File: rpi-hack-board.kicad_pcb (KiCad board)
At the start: 2 copper layers, 65 x 30 mm, 38 parts, among them J1 LOAD, J2 I2C_0, J3 I2C_1, J4 Raspberry_Pi_2_3, J5 PWR, J6 APA102, J7 SERIAL, J8 BREAKOUTS, Q1 TIP120, U1 DS1307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

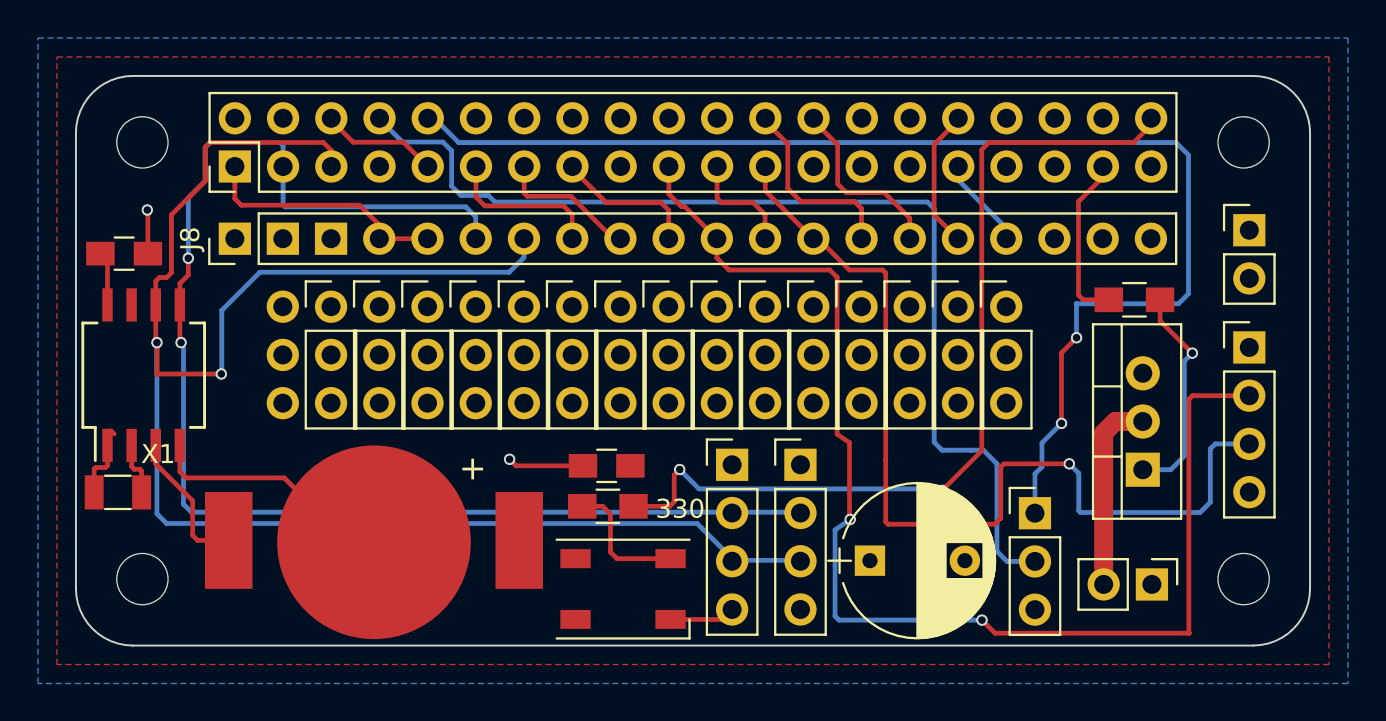
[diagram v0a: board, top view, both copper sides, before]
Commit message: Got a good start on the silkscreen layer, but there is loads to do.
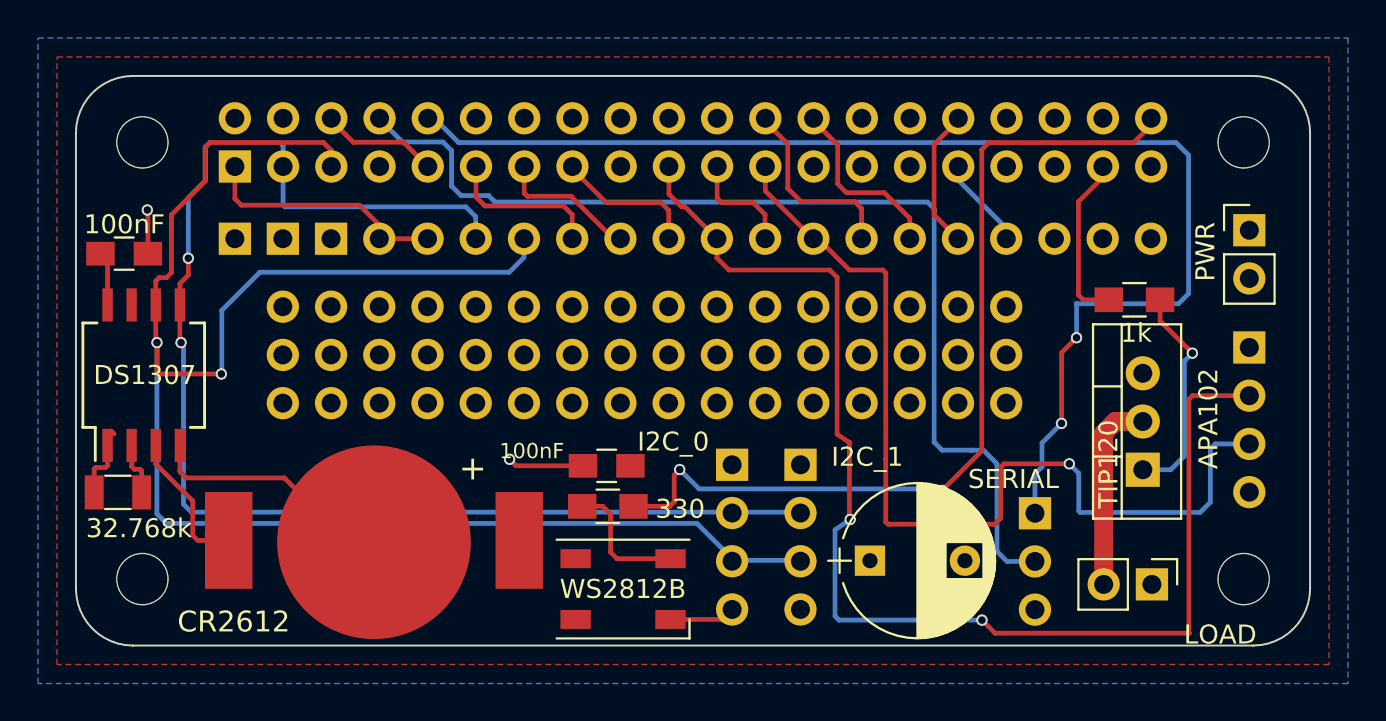
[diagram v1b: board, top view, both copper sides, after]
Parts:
- X1: value CRYSTAL -> 32.768k
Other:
- board text added: "5V"
- board text added: "CO"
- board text added: "CR2612"
- board text added: "GND"
- board text added: "RX"
- board text added: "SCL"
- board text added: "SDA"
- board text added: "SO"
- board text added: "TX"

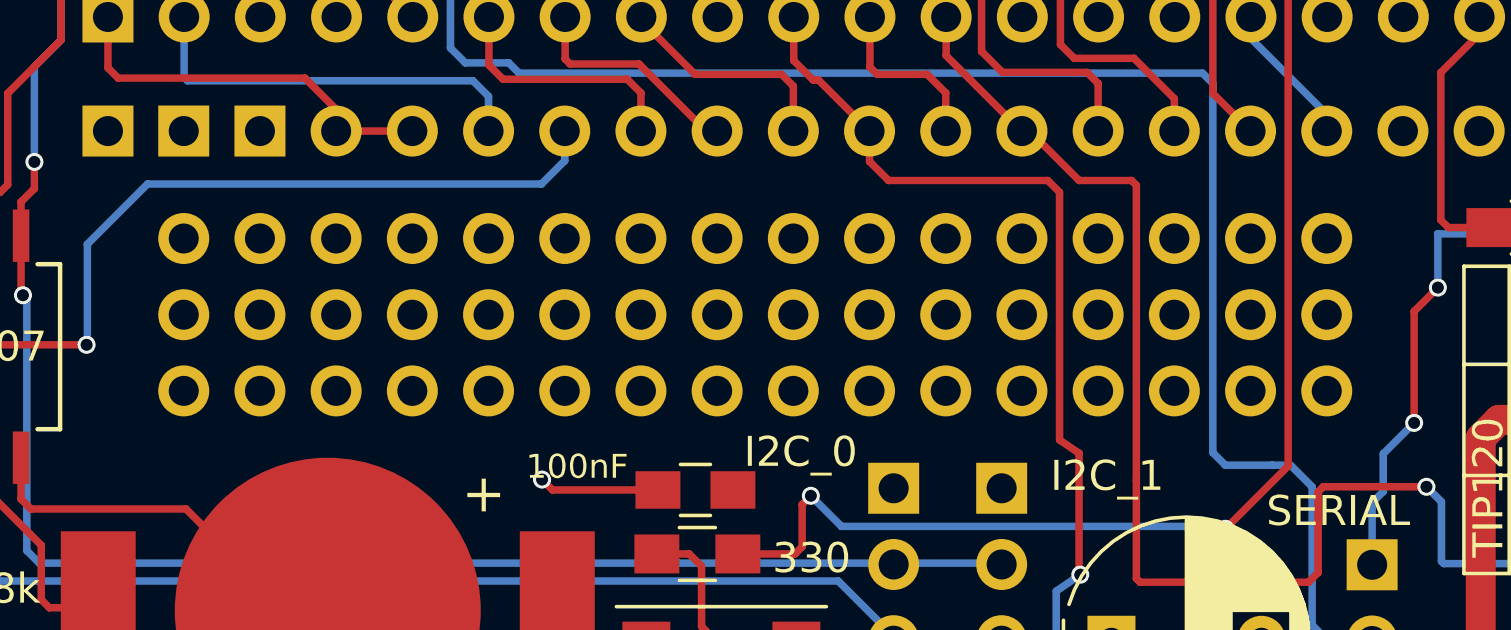
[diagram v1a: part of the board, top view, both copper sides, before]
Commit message: Connected all the prototyping lines
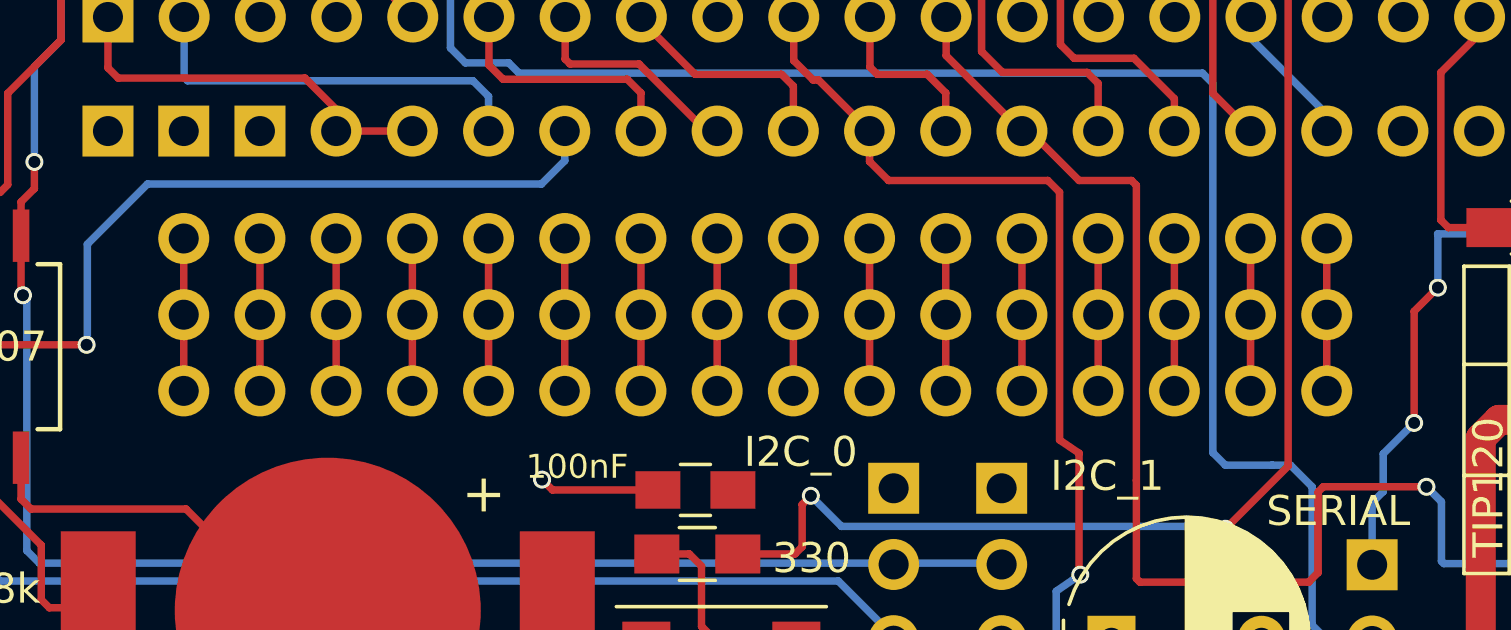
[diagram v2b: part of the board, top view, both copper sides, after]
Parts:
- REF**: footprint Pin_Headers:Pin_Header_Straight_1x03_Pitch2.54mm -> Prototype_Line_1x03_Pitch2.54mm
- REF** (x15): footprint Pin_Headers:Pin_Header_Straight_1x03_Pitch2.54mm -> mayhem-footprints:Prototype_Line_1x03_Pitch2.54mm

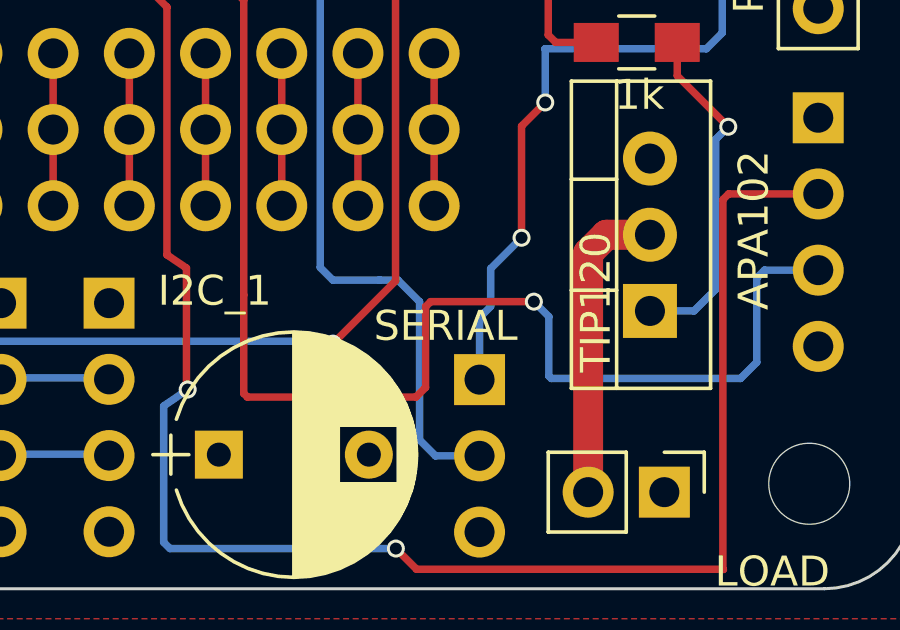
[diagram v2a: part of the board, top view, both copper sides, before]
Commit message: Most of the silkscreen looks good now
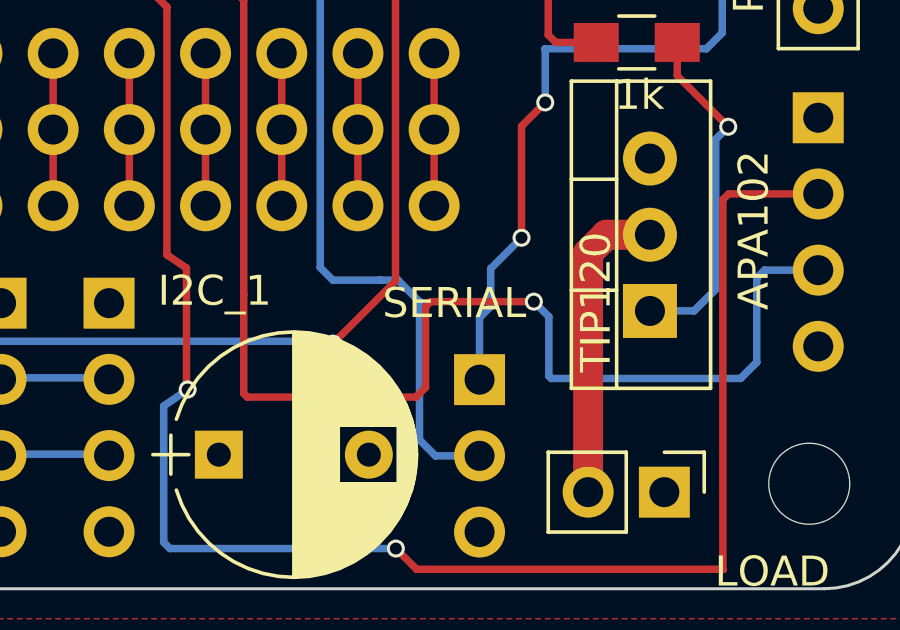
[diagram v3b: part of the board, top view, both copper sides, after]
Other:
- board text added: "APA102"
- board text added: "I2C_0"
- board text added: "I2C_1"
- board text added: "LOAD"
- board text added: "PWR"
- board text added: "SERIAL"
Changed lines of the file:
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@@
     (area 95.371429 98 169.628572 132.6747)
     (thickness 1.6)
-    (drawings 26)
+    (drawings 60)
     (tracks 261)
     (zones 0)
@@
   (page A4)
   (layers
-    (0 F.Cu signal)
+    (0 F.Cu signal hide)
     (31 B.Cu signal)
     (32 B.Adhes user hide)
@@
   )
   (setup
-    (last_trace_width 0.25)
+    (last_trace_width 1)
     (user_trace_width 0.5)
     (user_trace_width 1)
@@
     (pad_to_mask_clearance 0.2)
     (aux_axis_origin 0 0)
-    (visible_elements FFFFF77F)
+    (visible_elements FFFFF55F)
     (pcbplotparams
       (layerselection 0x00030_80000001)
@@
       (effects (font (size 1 1) (thickness 0.15)))
     )
-    (fp_text value SERIAL (at -1.13 -1.79) (layer F.SilkS)
+    (fp_text value SERIAL (at -0.84 -2.55) (layer F.SilkS)
       (effects (font (size 1 1) (thickness 0.15)))
     )
@@
     )
   )
-  (gr_text CO (at 159.43 119.3) (layer B.SilkS)
+  (gr_text GND (at 147.16 129.49) (layer B.SilkS)
     (effects (font (size 1 1) (thickness 0.15)) (justify mirror))
   )
-  (gr_text SO (at 159.37 117.01) (layer B.SilkS)
+  (gr_line (start 160.29 106.98) (end 160.63 106.98) (angle 90) (layer B.SilkS) (width 0.2))
+  (gr_line (start 160.29 111.67) (end 160.29 106.98) (angle 90) (layer B.SilkS) (width 0.2))
+  (gr_line (start 163.07 111.67) (end 160.29 111.67) (angle 90) (layer B.SilkS) (width 0.2))
+  (gr_line (start 163.07 106.95) (end 163.07 111.67) (angle 90) (layer B.SilkS) (width 0.2))
+  (gr_line (start 160.44 106.95) (end 163.07 106.95) (angle 90) (layer B.SilkS) (width 0.2))
+  (gr_line (start 160.55 122.99) (end 160.55 113.12) (angle 90) (layer B.SilkS) (width 0.2))
+  (gr_line (start 163.11 122.99) (end 160.55 122.99) (angle 90) (layer B.SilkS) (width 0.2))
+  (gr_line (start 163.11 113) (end 163.11 122.99) (angle 90) (layer B.SilkS) (width 0.2))
+  (gr_line (start 160.4 113) (end 163.11 113) (angle 90) (layer B.SilkS) (width 0.2))
+  (gr_line (start 158.04 124.97) (end 158.04 124.93) (angle 90) (layer B.SilkS) (width 0.2))
+  (gr_line (start 158.08 125.01) (end 158.04 124.97) (angle 90) (layer B.SilkS) (width 0.2))
+  (gr_line (start 152.51 125.01) (end 158.08 125.01) (angle 90) (layer B.SilkS) (width 0.2))
+  (gr_line (start 152.51 128.51) (end 152.51 125.01) (angle 90) (layer B.SilkS) (width 0.2))
+  (gr_line (start 158.12 128.51) (end 152.51 128.51) (angle 90) (layer B.SilkS) (width 0.2))
+  (gr_line (start 158.12 125.2) (end 158.12 128.51) (angle 90) (layer B.SilkS) (width 0.2))
+  (gr_line (start 149.09 121.76) (end 149.11 121.76) (angle 90) (layer B.SilkS) (width 0.2))
+  (gr_line (start 149.09 129.32) (end 149.09 121.76) (angle 90) (layer B.SilkS) (width 0.2))
+  (gr_line (start 151.83 129.32) (end 149.09 129.32) (angle 90) (layer B.SilkS) (width 0.2))
+  (gr_line (start 151.83 121.71) (end 151.83 129.32) (angle 90) (layer B.SilkS) (width 0.2))
+  (gr_line (start 149.06 121.71) (end 151.83 121.71) (angle 90) (layer B.SilkS) (width 0.2))
+  (gr_line (start 136.6 119.19) (end 137.24 119.19) (angle 90) (layer B.SilkS) (width 0.2))
+  (gr_line (start 136.6 129.53) (end 136.6 119.19) (angle 90) (layer B.SilkS) (width 0.2))
+  (gr_line (start 139.53 129.53) (end 136.6 129.53) (angle 90) (layer B.SilkS) (width 0.2))
+  (gr_line (start 139.53 119.11) (end 139.53 129.53) (angle 90) (layer B.SilkS) (width 0.2))
+  (gr_line (start 136.77 119.11) (end 139.53 119.11) (angle 90) (layer B.SilkS) (width 0.2))
+  (gr_line (start 133.06 119.27) (end 133.06 119.33) (angle 90) (layer B.SilkS) (width 0.2))
+  (gr_line (start 133.06 129.43) (end 133.06 119.27) (angle 90) (layer B.SilkS) (width 0.2))
+  (gr_line (start 135.95 129.43) (end 133.06 129.43) (angle 90) (layer B.SilkS) (width 0.2))
+  (gr_line (start 135.95 119.08) (end 135.95 129.43) (angle 90) (layer B.SilkS) (width 0.2))
+  (gr_line (start 133.18 119.08) (end 135.95 119.08) (angle 90) (layer B.SilkS) (width 0.2))
+  (gr_text 5V (at 156.77 129.28) (layer B.SilkS)
+    (effects (font (size 1 1) (thickness 0.15)) (justify mirror))
+  )
+  (gr_text PWR (at 163.9 109.23 90) (layer B.SilkS)
+    (effects (font (size 1 1) (thickness 0.2)) (justify mirror))
+  )
+  (gr_text APA102 (at 164.1 117.92 90) (layer B.SilkS)
+    (effects (font (size 1 1) (thickness 0.2)) (justify mirror))
+  )
+  (gr_text "LOAD\n" (at 156.97 124.25) (layer B.SilkS)
+    (effects (font (size 1 1) (thickness 0.2)) (justify mirror))
+  )
+  (gr_text SERIAL (at 149.51 120.42) (layer B.SilkS)
+    (effects (font (size 1 1) (thickness 0.2)) (justify mirror))
+  )
+  (gr_text I2C_1 (at 142.17 120.01) (layer B.SilkS)
+    (effects (font (size 1 1) (thickness 0.2)) (justify mirror))
+  )
+  (gr_text I2C_0 (at 128.99 124.28 90) (layer B.SilkS)
+    (effects (font (size 1 1) (thickness 0.2)) (justify mirror))
+  )
+  (gr_text CO (at 159.33 119.52) (layer B.SilkS)
+    (effects (font (size 1 1) (thickness 0.15)) (justify mirror))
+  )
+  (gr_text SO (at 159.26 116.96) (layer B.SilkS)
     (effects (font (size 1 1) (thickness 0.15)) (justify mirror))
   )
@@
     (effects (font (size 1 1) (thickness 0.15)) (justify mirror))
   )
-  (gr_text SCL (at 140.71 127.32) (layer B.SilkS)
-    (effects (font (size 1 1) (thickness 0.15)) (justify mirror))
-  )
   (gr_text SDA (at 131.88 123.05) (layer B.SilkS)
     (effects (font (size 1 1) (thickness 0.15)) (justify mirror))
   )
-  (gr_text RX (at 152.78 123.36) (layer B.SilkS)
+  (gr_text RX (at 147.93 122.14) (layer B.SilkS)
     (effects (font (size 1 1) (thickness 0.15)) (justify mirror))
   )
-  (gr_text TX (at 152.89 125.12) (layer B.SilkS)
+  (gr_text TX (at 147.85 127.22) (layer B.SilkS)
     (effects (font (size 1 1) (thickness 0.15)) (justify mirror))
   )
-  (gr_text GND (at 159.03 121.54) (layer B.SilkS)
+  (gr_text GND (at 158.84 121.65) (layer B.SilkS)
     (effects (font (size 1 1) (thickness 0.15)) (justify mirror))
   )
-  (gr_text GND (at 159.17 111.82) (layer B.SilkS)
+  (gr_text GND (at 158.65 110.6) (layer B.SilkS)
     (effects (font (size 1 1) (thickness 0.15)) (justify mirror))
   )
-  (gr_text GND (at 153.62 129) (layer B.SilkS)
+  (gr_text GND (at 153.77 129.27) (layer B.SilkS)
     (effects (font (size 1 1) (thickness 0.15)) (justify mirror))
   )
@@
     (effects (font (size 1 1) (thickness 0.15)) (justify mirror))
   )
-  (gr_text GND (at 140.73 128.92) (layer B.SilkS)
+  (gr_text 5V (at 159.18 108.05) (layer B.SilkS)
     (effects (font (size 1 1) (thickness 0.15)) (justify mirror))
   )
-  (gr_text 5V (at 160.21 106.21) (layer B.SilkS)
+  (gr_text 5V (at 159.41 113.54) (layer B.SilkS)
     (effects (font (size 1 1) (thickness 0.15)) (justify mirror))
   )
-  (gr_text 5V (at 159.66 113.23) (layer B.SilkS)
+  (gr_text 5V (at 130.42 120.64) (layer B.SilkS)
     (effects (font (size 1 1) (thickness 0.15)) (justify mirror))
   )
-  (gr_text SDA (at 140.76 122.49) (layer B.SilkS)
-    (effects (font (size 1 1) (thickness 0.15)) (justify mirror))
-  )
-  (gr_text 5V (at 140.7 120.3) (layer B.SilkS)
-    (effects (font (size 1 1) (thickness 0.15)) (justify mirror))
-  )
-  (gr_text 5V (at 132.26 119.45) (layer B.SilkS)
-    (effects (font (size 1 1) (thickness 0.15)) (justify mirror))
-  )

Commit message: Might be done!!
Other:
- board text added: "#05"
- board text added: "#07"
- board text added: "#08"
- board text added: "#12"
- board text added: "#17"
- board text added: "#22"
- board text added: "#27"
- board text added: "3.3V"
- board text added: "CLK"
- board text added: "RPi Zero/Zero-W Hack Board v2017-11-27 (c) Mayhem & Chaos 2017 http://mayhem.cat"
- board text added: "SI"
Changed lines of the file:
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@@
     (area 95.371429 98 169.628572 132.6747)
     (thickness 1.6)
-    (drawings 60)
+    (drawings 80)
     (tracks 261)
     (zones 0)
@@
     (35 F.Paste user hide)
     (36 B.SilkS user)
-    (37 F.SilkS user hide)
+    (37 F.SilkS user)
     (38 B.Mask user)
     (39 F.Mask user)
@@
   )
   (setup
-    (last_trace_width 1)
+    (last_trace_width 0.25)
     (user_trace_width 0.5)
     (user_trace_width 1)
@@
     (pad_to_mask_clearance 0.2)
     (aux_axis_origin 0 0)
-    (visible_elements FFFFF55F)
+    (visible_elements FFFFF75F)
     (pcbplotparams
       (layerselection 0x00030_80000001)
@@
     )
   )
+  (gr_text GND (at 156.67 110.28) (layer F.SilkS)
+    (effects (font (size 0.8 0.8) (thickness 0.15)))
+  )
+  (gr_text GND (at 151.62 110.29) (layer F.SilkS)
+    (effects (font (size 0.8 0.8) (thickness 0.15)))
+  )
+  (gr_text GND (at 154.15 110.26) (layer F.SilkS)
+    (effects (font (size 0.8 0.8) (thickness 0.15)))
+  )
+  (gr_text "#05" (at 149.03 110.38) (layer F.SilkS)
+    (effects (font (size 0.8 0.8) (thickness 0.15)))
+  )
+  (gr_text "#12" (at 146.43 110.36) (layer F.SilkS)
+    (effects (font (size 0.8 0.8) (thickness 0.15)))
+  )
+  (gr_text "#07" (at 143.95 110.36) (layer F.SilkS)
+    (effects (font (size 0.8 0.8) (thickness 0.15)))
+  )
+  (gr_text "#08" (at 141.41 110.38) (layer F.SilkS)
+    (effects (font (size 0.8 0.8) (thickness 0.15)))
+  )
+  (gr_text CLK (at 138.93 110.42) (layer F.SilkS)
+    (effects (font (size 0.8 0.8) (thickness 0.15)))
+  )
+  (gr_text SO (at 136.27 110.4) (layer F.SilkS)
+    (effects (font (size 0.8 0.8) (thickness 0.15)))
+  )
+  (gr_text SI (at 133.73 110.4) (layer F.SilkS)
+    (effects (font (size 0.8 0.8) (thickness 0.15)))
+  )
+  (gr_text "#22" (at 131.19 110.42) (layer F.SilkS)
+    (effects (font (size 0.8 0.8) (thickness 0.15)))
+  )
+  (gr_text "#27" (at 128.75 110.38) (layer F.SilkS)
+    (effects (font (size 0.8 0.8) (thickness 0.15)))
+  )
+  (gr_text "#17" (at 126.41 110.4) (layer F.SilkS)
+    (effects (font (size 0.8 0.8) (thickness 0.15)))
+  )
+  (gr_text SCL (at 123.75 110.38) (layer F.SilkS)
+    (effects (font (size 0.8 0.8) (thickness 0.15)))
+  )
+  (gr_text SDA (at 121.01 110.38) (layer F.SilkS)
+    (effects (font (size 0.8 0.8) (thickness 0.15)))
+  )
+  (gr_text 3.3V (at 117.31 110.34) (layer F.SilkS)
+    (effects (font (size 1 1) (thickness 0.2)))
+  )
+  (gr_text 5V (at 113.45 110.38) (layer F.SilkS)
+    (effects (font (size 1 1) (thickness 0.2)))
+  )
+  (gr_text 5V (at 110.83 110.4) (layer F.SilkS)
+    (effects (font (size 1 1) (thickness 0.2)))
+  )
+  (gr_text 5V (at 108.31 110.34) (layer F.SilkS)
+    (effects (font (size 1 1) (thickness 0.2)))
+  )
+  (gr_text "RPi Zero/Zero-W Hack Board\nv2017-11-27\n(c) Mayhem & Chaos 2017\nhttp://mayhem.cat" (at 126.51 122.82) (layer B.SilkS)
+    (effects (font (size 1.1 1.1) (thickness 0.2)) (justify left mirror))
+  )
   (gr_text GND (at 147.16 129.49) (layer B.SilkS)
